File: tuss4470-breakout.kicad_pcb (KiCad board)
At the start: 4 copper layers, 27.9 x 31.8 mm, 23 parts, among them J1 Screw_Terminal_01x02, J2 Conn_01x08_Pin, J3 Conn_01x08_Pin, J4 Screw_Terminal_01x02, U1 LP5907MFX-3.3, U2 TUSS4470

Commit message: generate gerbers
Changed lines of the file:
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@@
 			(outputformat 1)
 			(mirror no)
-			(drillshape 1)
+			(drillshape 0)
 			(scaleselection 1)
-			(outputdirectory "")
+			(outputdirectory "gerbers/")
 		)
 	)
@@
 		)
 		(property "Value" "100n"
-			(at 0 1.43 0)
+			(at 0.254 1.43 0)
 			(layer "F.Fab")
 			(effects
@@
 		(tags "WQFN NoLead Maxim_T2044-5C Maxim_20L-TQFN-4x4x0.75mm Texas_RTJ0020D")
 		(property "Reference" "U2"
-			(at -2.286 3.175 180)
+			(at -3.429 0.127 180)
 			(layer "F.SilkS")
 			(effects
@@
 		)
 		(property "Value" "TUSS4470"
-			(at 0 3.330001 90)
+			(at -2.794 0.762 180)
 			(layer "F.Fab")
 			(effects
@@
 		(tags "resistor")
 		(property "Reference" "R3"
-			(at -2.9265 -0.066001 90)
+			(at 2.5345 -0.066001 90)
 			(layer "F.SilkS")
 			(effects
@@
 		)
 		(property "Value" "0"
-			(at 0 1.43 90)
+			(at 1.8995 0 90)
 			(layer "F.Fab")
 			(effects
@@
 		)
 		(property "Value" "100n"
-			(at 0 1.43 0)
+			(at 3.302 0 0)
 			(layer "F.Fab")
 			(effects
@@
 		)
 		(property "Value" "2u"
-			(at 0 1.43 0)
+			(at 2.54 0 0)
 			(layer "F.Fab")
 			(effects
@@
 		)
 		(property "Value" "2u"
-			(at 0 1.43 0)
+			(at 0 -1.016 0)
 			(layer "F.Fab")
 			(effects
@@
 		)
 		(property "Value" "200"
-			(at 0 1.43 0)
+			(at -2.667 0 0)
 			(layer "F.Fab")
 			(effects
@@
 		)
 		(property "Value" "16n"
-			(at 0 1.43 0)
+			(at 3.175 0 0)
 			(layer "F.Fab")
 			(effects
@@
 		)
 		(property "Value" "2u"
-			(at 0 1.43 0)
+			(at 0 -1.349 0)
 			(layer "F.Fab")
 			(effects
@@
 		)
 		(property "Value" "0"
-			(at 0 1.43 90)
+			(at -1.8995 0 90)
 			(layer "F.Fab")
 			(effects
@@
 		)
 		(property "Value" "MountingHole"
-			(at 0 4.15 0)
+			(at 0 0 0)
 			(layer "F.Fab")
 			(effects
@@
 		)
 		(property "Value" "10"
-			(at 0 1.43 90)
+			(at 0.127 1.397 90)
 			(layer "F.Fab")
 			(effects
@@
 		(tags "SOT TO_SOT_SMD")
 		(property "Reference" "U1"
-			(at 0.048 2.521 90)
+			(at -0.127 -2.794 180)
 			(layer "F.SilkS")
 			(effects
@@
 		)
 		(property "Value" "LP5907MFX-3.3"
-			(at 0 2.4 90)
+			(at -1.397 -0.254 180)
 			(layer "F.Fab")
 			(effects
@@
 		)
 		(property "Value" "Screw_Terminal_01x02"
-			(at 1.27 4.52 0)
+			(at 1.27 5.08 0)
 			(layer "F.Fab")
 			(effects
@@
 		)
 		(property "Value" "MountingHole"
-			(at 0 4.15 0)
+			(at 0 0 0)
 			(layer "F.Fab")
 			(effects
@@
 		)
 		(property "Value" "VPWR SEL"
-			(at 0 7.460001 0)
+			(at 2.413 3.048 90)
 			(layer "F.Fab")
 			(effects
@@
 		(tags "resistor")
 		(property "Reference" "R1"
-			(at -0.889 -1.651 180)
+			(at -0.889 -1.905 180)
 			(layer "F.SilkS")
 			(effects
@@
 		)
 		(property "Value" "1N4001"
-			(at 0 2.1 90)
+			(at -0.05 1.651 90)
 			(layer "F.Fab")
 			(effects
@@
 		)
 		(fp_text user "${REFERENCE}"
-			(at 0 -2.000001 90)
+			(at 2.159 0 90)
 			(layer "F.Fab")
 			(effects
@@
 		)
 		(property "Value" "330p"
-			(at 0 1.43 90)
+			(at 0 -1.308 90)
 			(layer "F.Fab")
 			(effects
@@
 	)
 	(segment
-		(start 86.503 50.6035)
-		(end 86.503 51.053)
-		(width 0.3)
-		(layer "F.Cu")
-		(net "OUT3")
-	)
-	(segment
-		(start 86.503 51.053)
-		(end 86.233 51.323)
-		(width 0.3)
-		(layer "F.Cu")
-		(net "OUT3")
-	)
-	(via
-		(at 86.233 51.323)
-		(size 0.6)
-		(drill 0.3)
-		(layers "F.Cu" "B.Cu")
-		(net "OUT3")
-	)
-	(segment
-		(start 98.537 51.323)
-		(end 99.06 50.8)
-		(width 0.3)
-		(layer "B.Cu")
-		(net "OUT3")
-	)
-	(segment
-		(start 86.233 51.323)
-		(end 98.537 51.323)
-		(width 0.3)
-		(layer "B.Cu")
-		(net "OUT3")
-	)
-	(segment
 		(start 81.775 47.752)
 		(end 81.673 47.854)
@@
 	)
 	(segment
+		(start 86.503 50.6035)
+		(end 86.503 51.053)
+		(width 0.3)
+		(layer "F.Cu")
+		(net "OUT3")
+	)
+	(segment
+		(start 86.503 51.053)
+		(end 86.233 51.323)
+		(width 0.3)
+		(layer "F.Cu")
+		(net "OUT3")
+	)
+	(via
+		(at 86.233 51.323)
+		(size 0.6)
+		(drill 0.3)
+		(layers "F.Cu" "B.Cu")
+		(net "OUT3")
+	)
+	(segment
+		(start 98.537 51.323)
+		(end 99.06 50.8)
+		(width 0.3)
+		(layer "B.Cu")
+		(net "OUT3")
+	)
+	(segment
+		(start 86.233 51.323)
+		(end 98.537 51.323)
+		(width 0.3)
+		(layer "B.Cu")
+		(net "OUT3")
+	)
+	(segment
 		(start 87.503 50.6035)
 		(end 87.503 53.824999)
@@
 	)
 	(segment
+		(start 85.5405 38.9195)
+		(end 86.36 38.1)
+		(width 0.3)
+		(layer "F.Cu")
+		(net "Net-(J4-Pin_2)")
+	)
+	(segment
+		(start 85.5405 47.641)
+		(end 85.5405 38.9195)
+		(width 0.3)
+		(layer "F.Cu")
+		(net "Net-(J4-Pin_2)")
+	)
+	(segment
 		(start 85.042905 48.141001)
 		(end 83.325 46.423096)
@@
 	)
 	(segment
+		(start 90.490001 56.6995)
+		(end 90.3665 56.6995)
+		(width 0.3)
+		(layer "F.Cu")
+		(net "3V3")
+	)
+	(segment
+		(start 90.424 56.765501)
+		(end 90.490001 56.6995)
+		(width 0.3)
+		(layer "F.Cu")
+		(net "3V3")
+	)
+	(segment
+		(start 90.424 57.404)
+		(end 90.424 56.765501)
+		(width 0.3)
+		(layer "F.Cu")
+		(net "3V3")
+	)
+	(via
+		(at 90.424 57.404)
+		(size 0.6)
+		(drill 0.3)
+		(layers "F.Cu" "B.Cu")
+		(net "3V3")
+	)
+	(segment
+		(start 79.756 57.404)
+		(end 90.424 57.404)
+		(width 0.3)
+		(layer "B.Cu")
+		(net "3V3")
+	)
+	(segment
+		(start 76.2 60.96)
+		(end 79.756 57.404)
+		(width 0.3)
+		(layer "B.Cu")
+		(net "3V3")
+	)
+	(segment
 		(start 93.919001 62.283001)
 		(end 94.12 62.484)
@@
 		(net "VPWR")
 	)
-	(segment
-		(start 90.490001 56.6995)
-		(end 90.3665 56.6995)
-		(width 0.3)
-		(layer "F.Cu")
-		(net "3V3")
-	)
-	(segment
-		(start 90.424 56.765501)
-		(end 90.490001 56.6995)
-		(width 0.3)
-		(layer "F.Cu")
-		(net "3V3")
-	)
-	(segment
-		(start 90.424 57.404)
-		(end 90.424 56.765501)
-		(width 0.3)
-		(layer "F.Cu")
-		(net "3V3")
-	)
-	(via
-		(at 90.424 57.404)
-		(size 0.6)
-		(drill 0.3)
-		(layers "F.Cu" "B.Cu")
-		(net "3V3")
-	)
-	(segment
-		(start 79.756 57.404)
-		(end 90.424 57.404)
-		(width 0.3)
-		(layer "B.Cu")
-		(net "3V3")
-	)
-	(segment
-		(start 76.2 60.96)
-		(end 79.756 57.404)
-		(width 0.3)
-		(layer "B.Cu")
-		(net "3V3")
-	)
-	(segment
-		(start 85.5405 38.9195)
-		(end 86.36 38.1)
-		(width 0.3)
-		(layer "F.Cu")
-		(net "Net-(J4-Pin_2)")
-	)
-	(segment
-		(start 85.5405 47.641)
-		(end 85.5405 38.9195)
-		(width 0.3)
-		(layer "F.Cu")
-		(net "Net-(J4-Pin_2)")
-	)
 	(zone

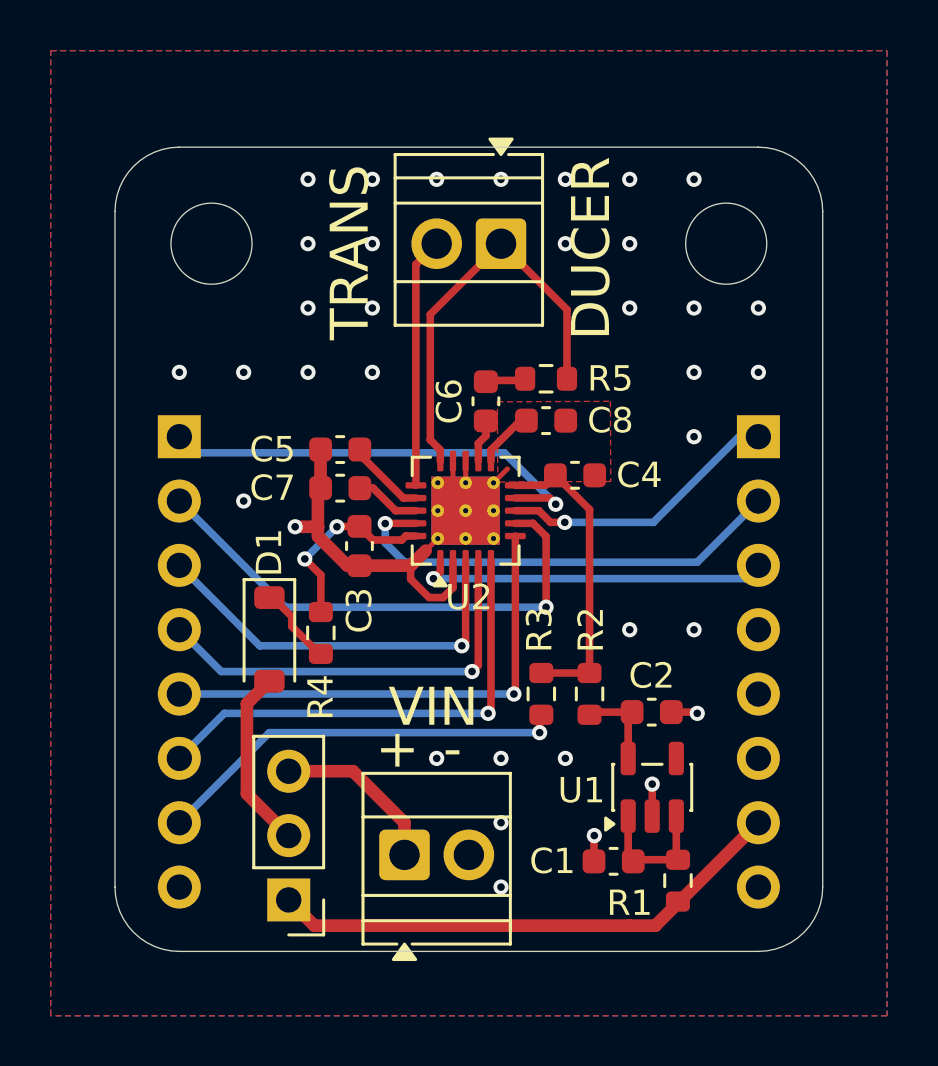
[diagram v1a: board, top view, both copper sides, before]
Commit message: v0.1 ordered pcb and components
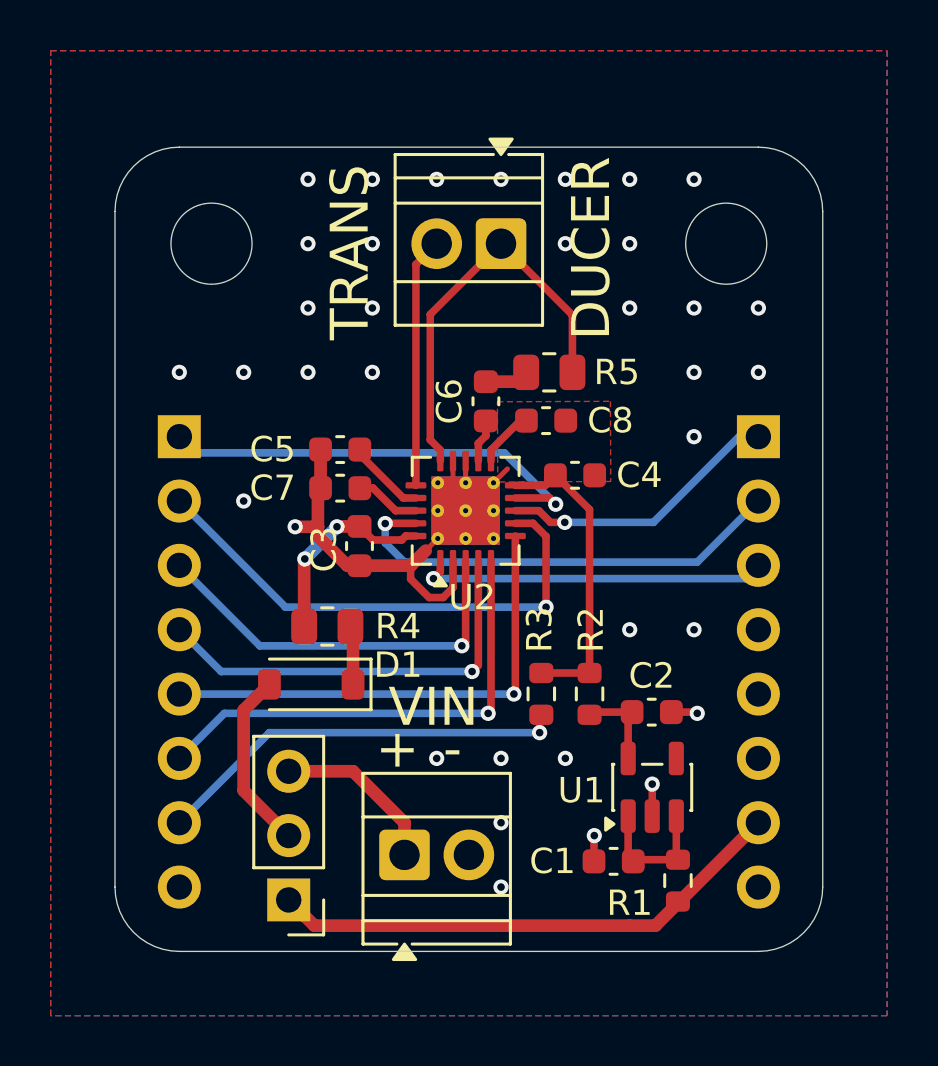
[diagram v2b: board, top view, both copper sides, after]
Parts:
- C7: value 16n -> 15n
- D1: value 1N4001 -> 1N5819HW-7-F
- R4, R5: footprint Resistor_SMD:R_0603_1608Metric -> Resistor_SMD:R_0805_2012Metric
- moved D1 2.43 mm to (81.4, 55.5), turned to 180 degrees
- moved R4 0.36 mm to (82.0, 53.2), turned to 180 degrees
- moved R5 0.28 mm to (90.8, 43.2)
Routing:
- net Net-(D1-K): track 3.18 -> 2.33 mm
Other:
- board text added: "tuss4470-breakout v0.1"
